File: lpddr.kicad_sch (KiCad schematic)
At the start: 2 parts, among them U1 MPFS250T-FCVG484, U11 MT53D512M32D2_WFBGA

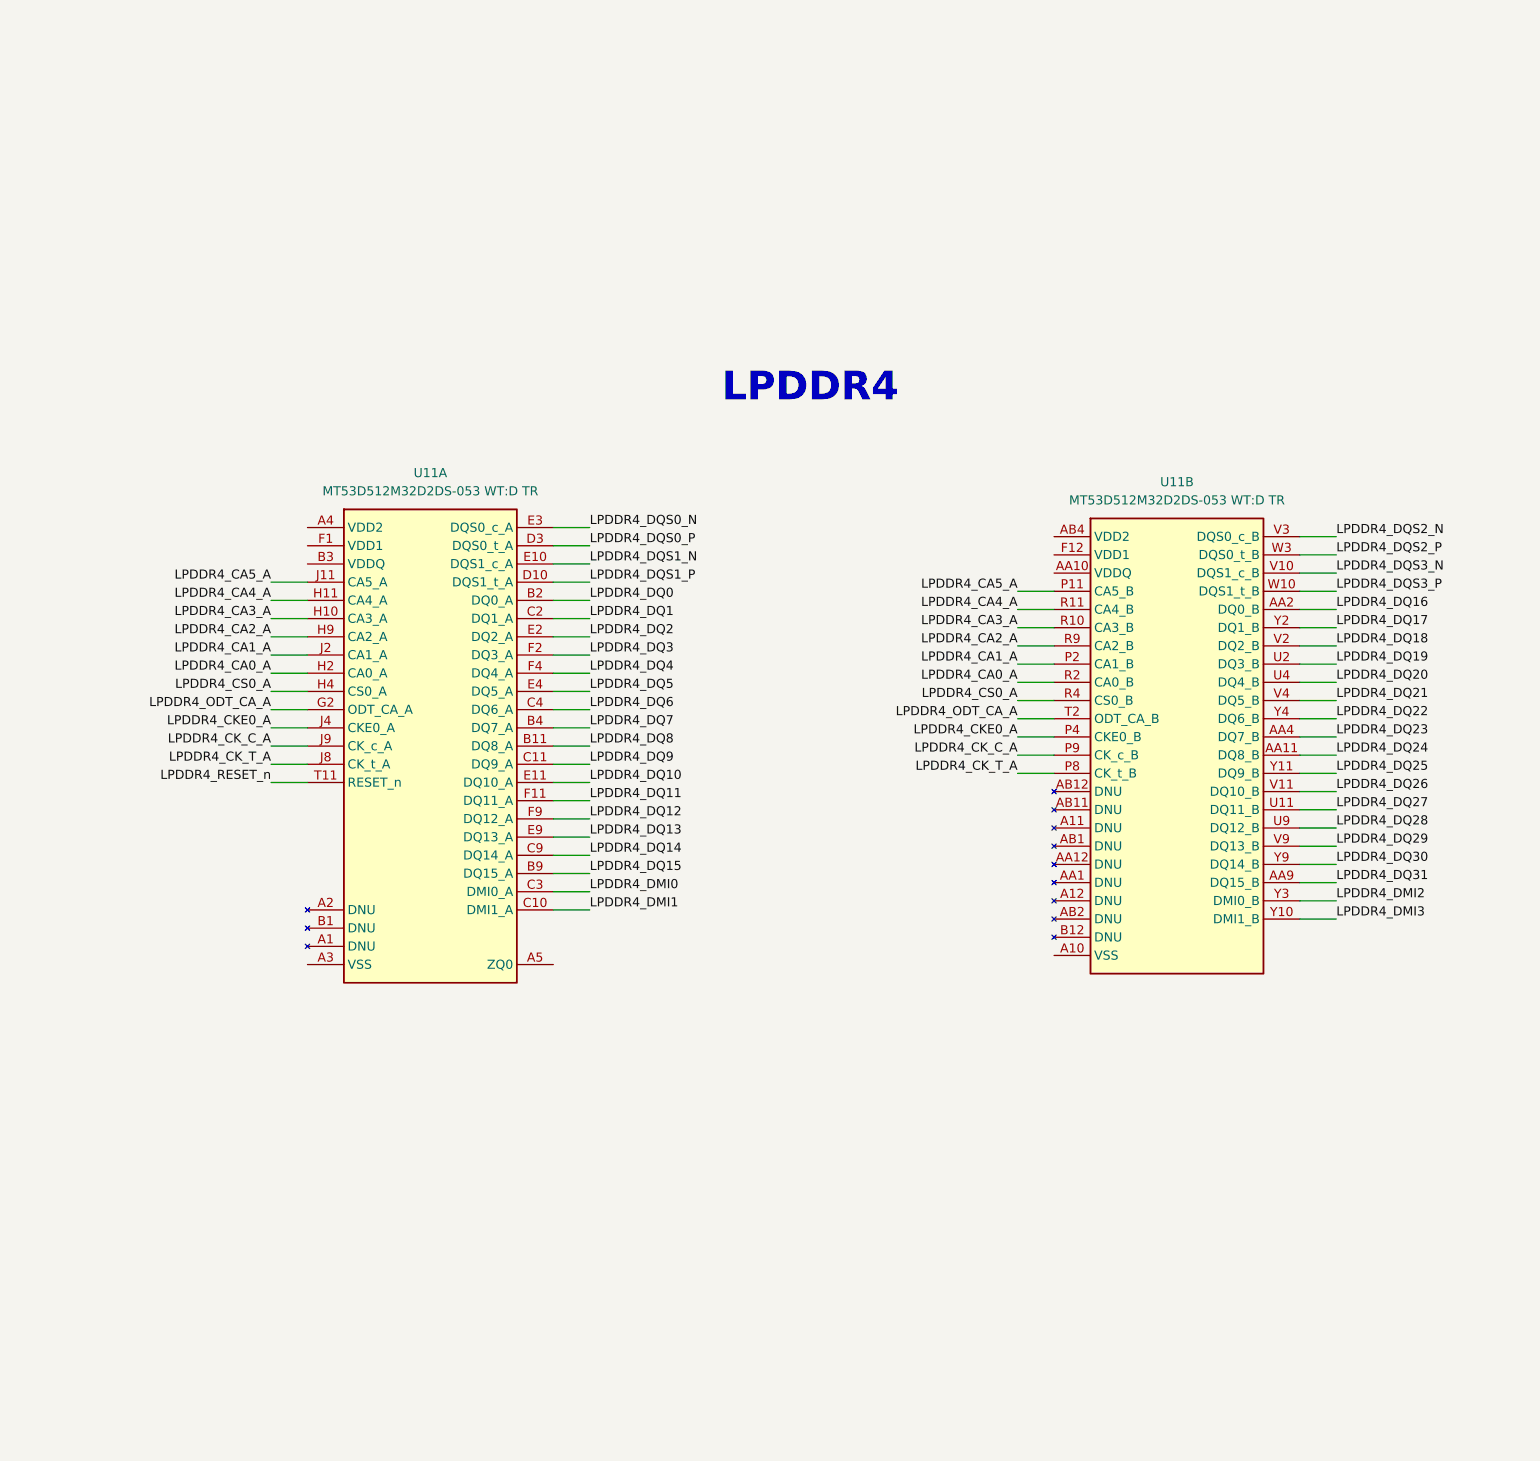
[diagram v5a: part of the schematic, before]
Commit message: [#54491] Add decoupling capacitors to LPDDR4
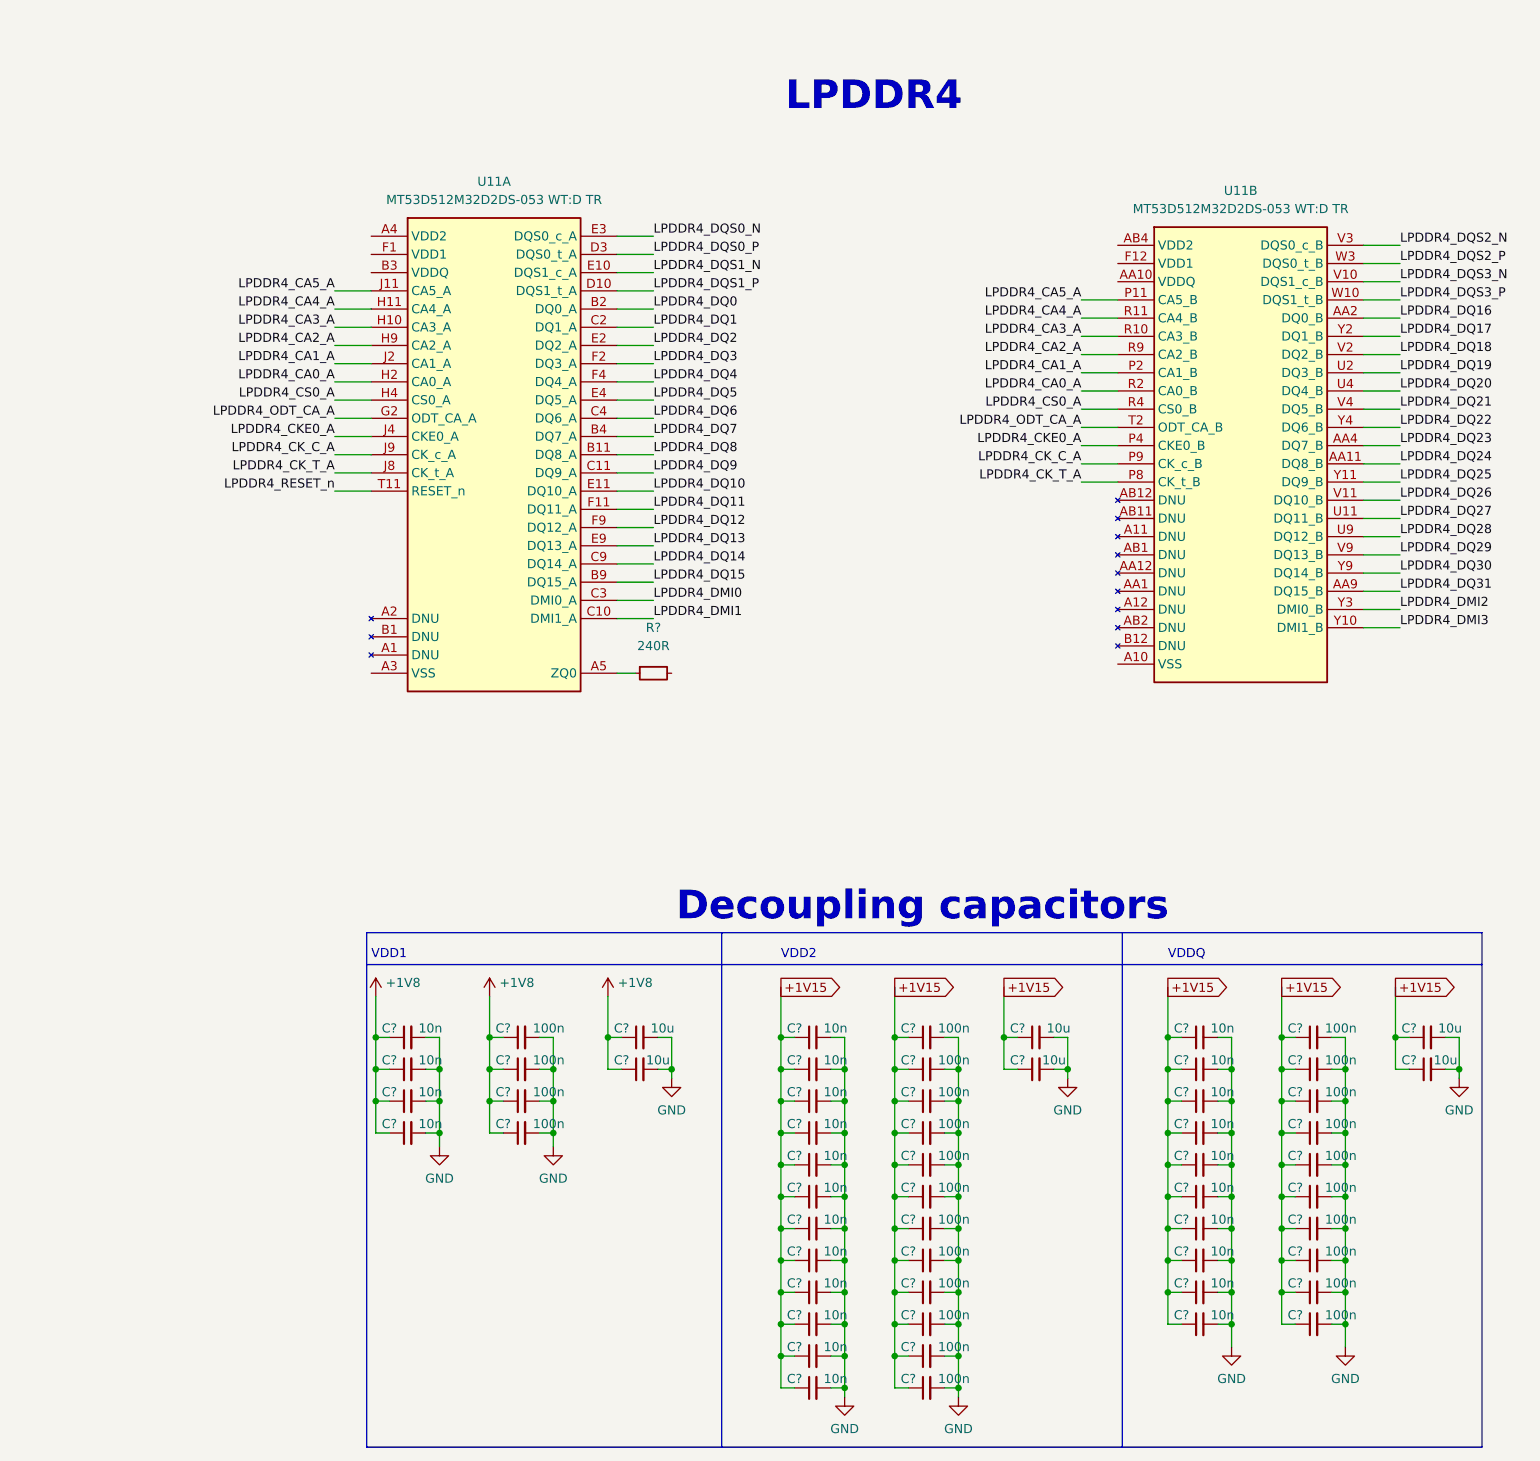
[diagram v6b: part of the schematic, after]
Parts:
- added C? (x26): C_100n_0402, antmicro-footprints:C_0402_1005Metric, symbol antmicroCapacitors0402:C_100n_0402
- added C? (x26): C_10n_0402, antmicro-footprints:C_0402_1005Metric, symbol antmicroCapacitors0402:C_10n_0402
- added C? (x6): C_10u_0402, antmicro-footprints:C_0402_1005Metric, symbol antmicroCapacitors0402:C_10u_0402
- added R?: R_240R_0402, antmicro-footprints:R_0402_1005Metric, symbol antmicroResistors0402:R_240R_0402
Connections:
- net at U11.A5 (ZQ0): now also R?.1
- new net +1V15: C?.1, C?.1, C?.1, C?.1, C?.1, C?.1, C?.1, C?.1, C?.1, C?.1, C?.1, C?.1, C?.1, C?.1, C?.1, C?.1, C?.1, C?.1, C?.1, C?.1, C?.1, C?.1, C?.1, C?.1, C?.1, C?.1, C?.1, C?.1, C?.1, C?.1, C?.1, C?.1, C?.1, C?.1, C?.1, C?.1, C?.1, C?.1, C?.1, C?.1, C?.1, C?.1, C?.1, C?.1, C?.1, C?.1, C?.1, C?.1
- new net +1V8: C?.1, C?.1, C?.1, C?.1, C?.1, C?.1, C?.1, C?.1, C?.1, C?.1
- new net GND: C?.2, C?.2, C?.2, C?.2, C?.2, C?.2, C?.2, C?.2, C?.2, C?.2, C?.2, C?.2, C?.2, C?.2, C?.2, C?.2, C?.2, C?.2, C?.2, C?.2, C?.2, C?.2, C?.2, C?.2, C?.2, C?.2, C?.2, C?.2, C?.2, C?.2, C?.2, C?.2, C?.2, C?.2, C?.2, C?.2, C?.2, C?.2, C?.2, C?.2, C?.2, C?.2, C?.2, C?.2, C?.2, C?.2, C?.2, C?.2, C?.2, C?.2, C?.2, C?.2, C?.2, C?.2, C?.2, C?.2, C?.2, C?.2
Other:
- note added: "Decoupling capacitors"
- note added: "VDD1"
- note added: "VDD2"
- note added: "VDDQ"
- moved on the sheet: U11A, U11B

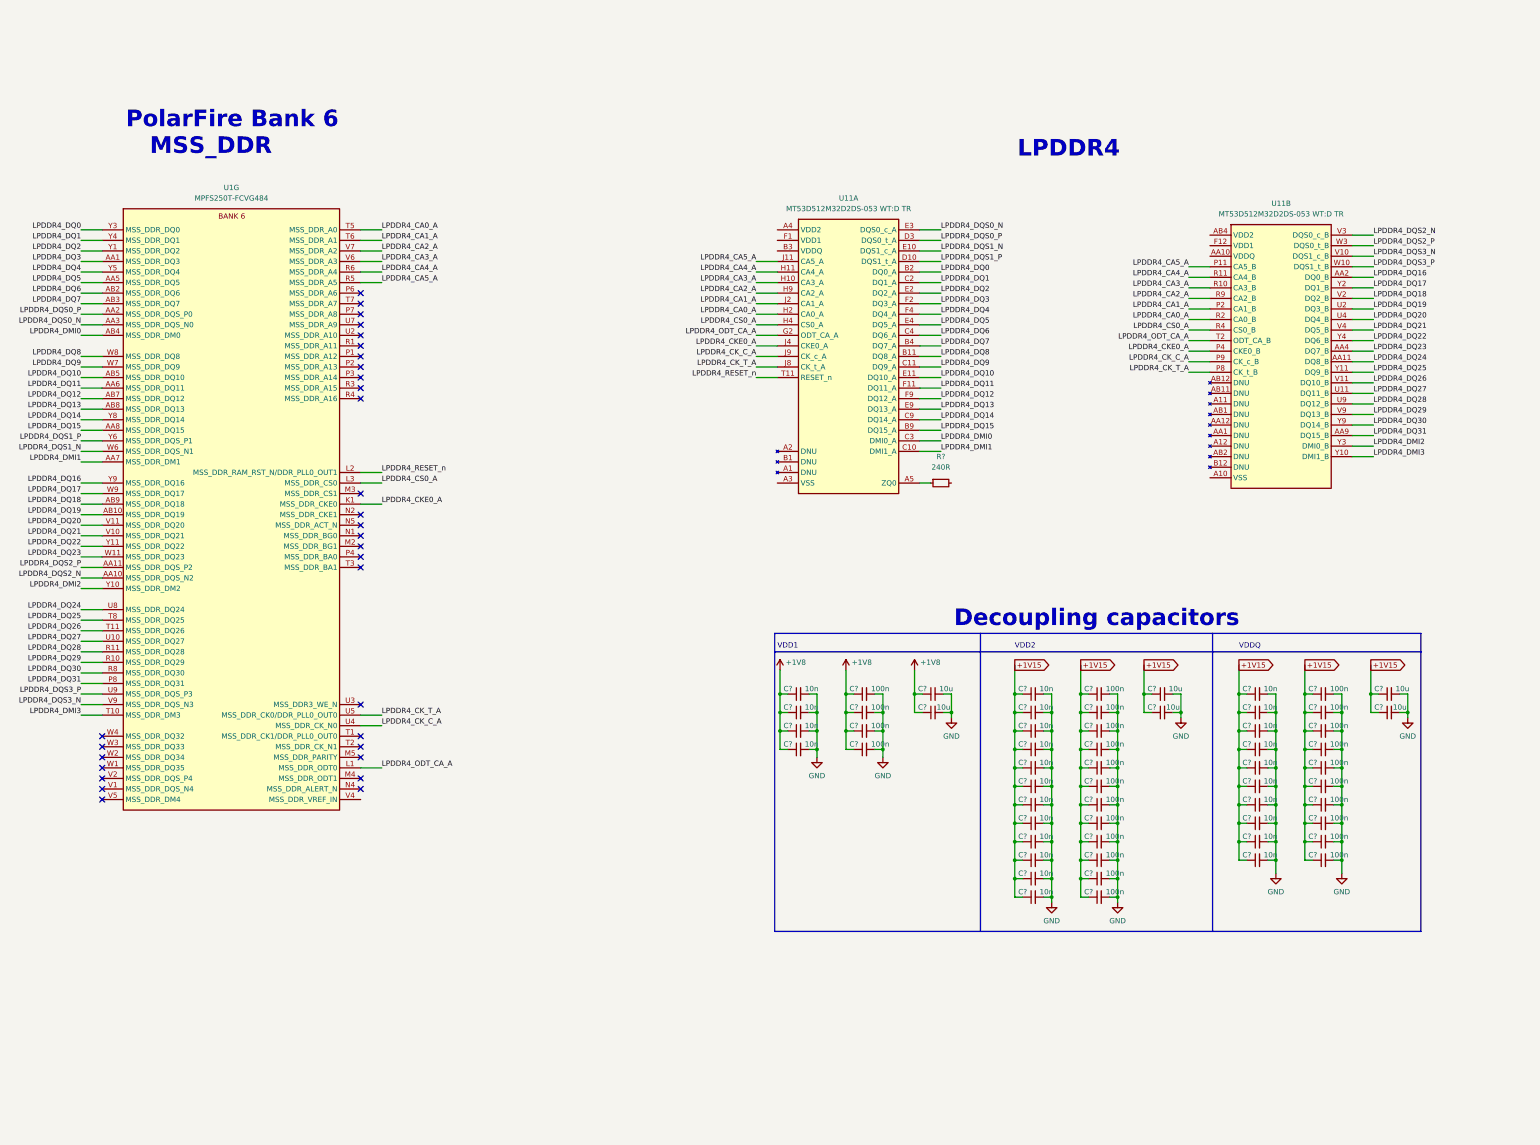
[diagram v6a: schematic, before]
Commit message: [#54491] Provide power for LPDDR4
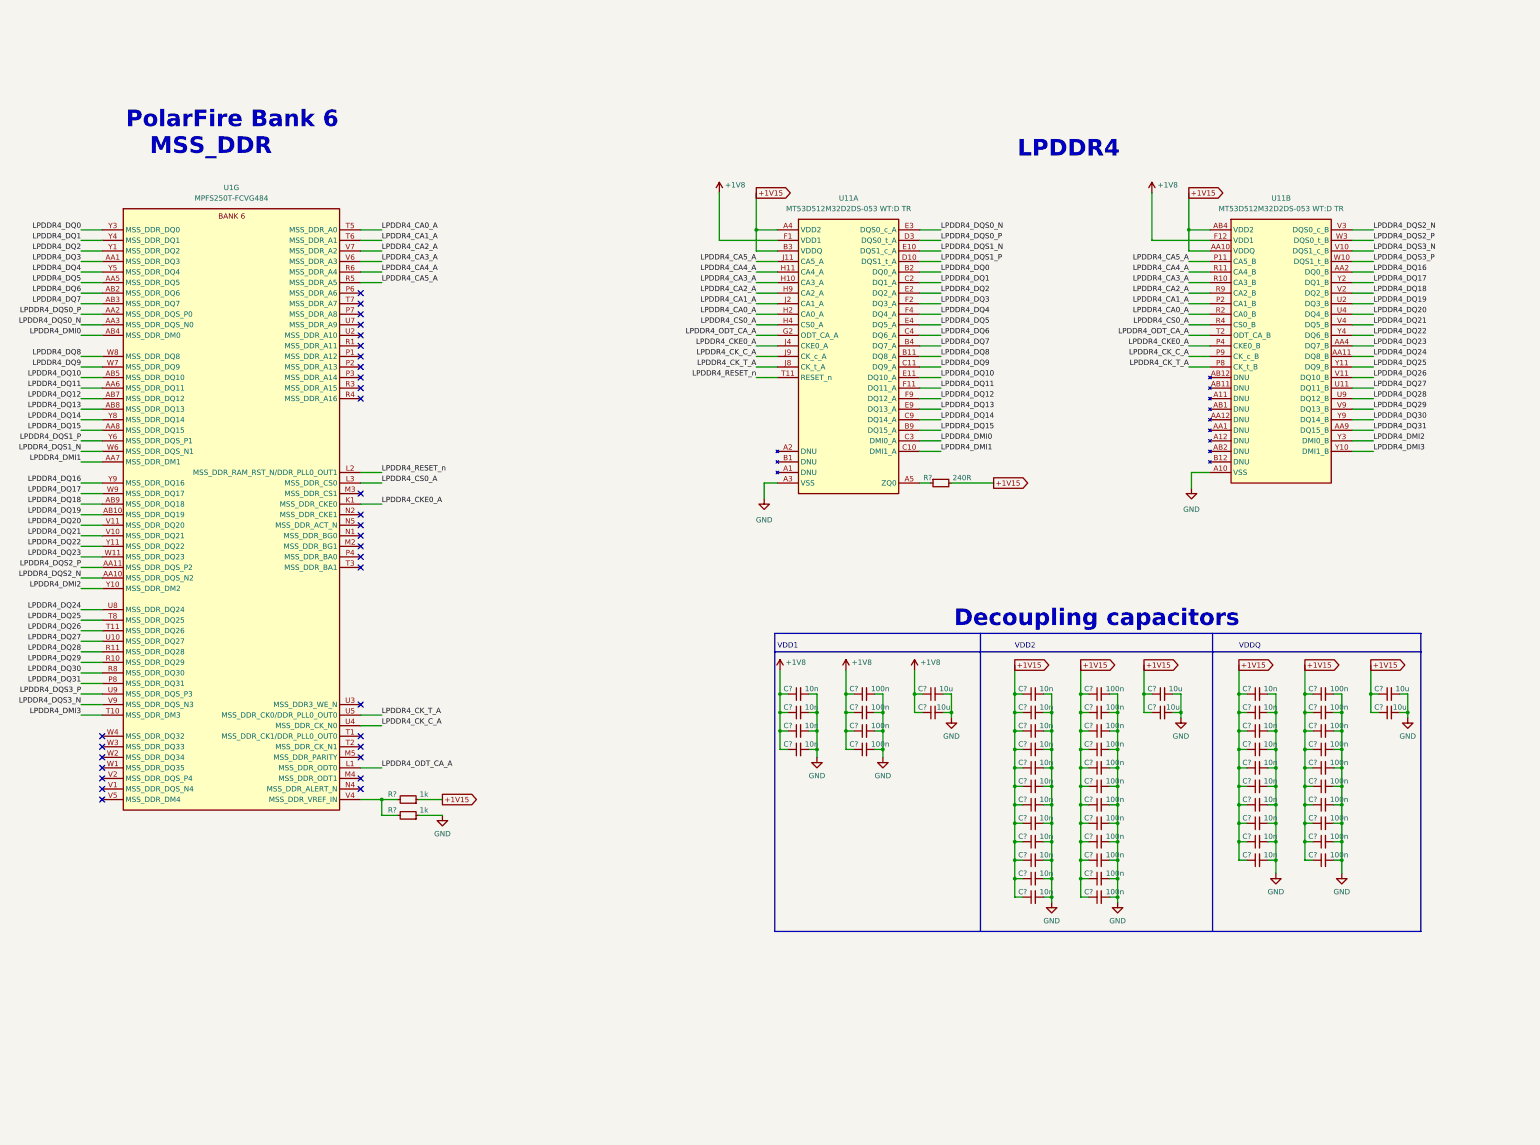
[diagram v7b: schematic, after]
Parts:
- added R? (x2): R_1k_0402, antmicro-footprints:R_0402_1005Metric, symbol antmicroResistors0402:R_1k_0402
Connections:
- net +1V15: now also R?.2, U11.A4 (VDD2), U11.A9 (VDD2), U11.AA10 (VDDQ), U11.AA3 (VDDQ), U11.AA5 (VDDQ), U11.AA8 (VDDQ), U11.AB4 (VDD2), U11.AB9 (VDD2), U11.B10 (VDDQ), U11.B3 (VDDQ), U11.B5 (VDDQ), U11.B8 (VDDQ), U11.D1 (VDDQ), U11.D12 (VDDQ), U11.D5 (VDDQ), U11.D8 (VDDQ), U11.F10 (VDDQ), U11.F3 (VDDQ), U11.F5 (VDD2), U11.F8 (VDD2), U11.H1 (VDD2), U11.H12 (VDD2), U11.H5 (VDD2), U11.H8 (VDD2), U11.K1 (VDD2), U11.K10 (VDD2), U11.K12 (VDD2), U11.K3 (VDD2), U11.N1 (VDD2), U11.N10 (VDD2), U11.N12 (VDD2), U11.N3 (VDD2), U11.R1 (VDD2), U11.R12 (VDD2), U11.R5 (VDD2), U11.R8 (VDD2), U11.U10 (VDDQ), U11.U3 (VDDQ), U11.U5 (VDD2), U11.U8 (VDD2), U11.W1 (VDDQ), U11.W12 (VDDQ), U11.W5 (VDDQ), U11.W8 (VDDQ), R?.1
- net +1V8: now also U11.F1 (VDD1), U11.F12 (VDD1), U11.G4 (VDD1), U11.G9 (VDD1), U11.T4 (VDD1), U11.T9 (VDD1), U11.U1 (VDD1), U11.U12 (VDD1)
- net GND: now also U11.A10 (VSS), U11.A3 (VSS), U11.AB10 (VSS), U11.AB3 (VSS), U11.AB5 (VSS), U11.AB8 (VSS), U11.C1 (VSS), U11.C12 (VSS), U11.C5 (VSS), U11.C8 (VSS), U11.D11 (VSS), U11.D2 (VSS), U11.D4 (VSS), U11.D9 (VSS), U11.E1 (VSS), U11.E12 (VSS), U11.E5 (VSS), U11.E8 (VSS), U11.G1 (VSS), U11.G10 (VSS), U11.G12 (VSS), U11.G3 (VSS), U11.G5 (VSS), U11.G8 (VSS), U11.J1 (VSS), U11.J10 (VSS), U11.J12 (VSS), U11.J3 (VSS), U11.K11 (VSS), U11.K2 (VSS), U11.K4 (VSS), U11.K9 (VSS), U11.N11 (VSS), U11.N2 (VSS), U11.N4 (VSS), U11.N9 (VSS), U11.P1 (VSS), U11.P10 (VSS), U11.P12 (VSS), U11.P3 (VSS), U11.T1 (VSS), U11.T10 (VSS), U11.T12 (VSS), U11.T3 (VSS), U11.T5 (VSS), U11.T8 (VSS), U11.V1 (VSS), U11.V12 (VSS), U11.V5 (VSS), U11.V8 (VSS), U11.W11 (VSS), U11.W2 (VSS), U11.W4 (VSS), U11.W9 (VSS), U11.Y1 (VSS), U11.Y12 (VSS), U11.Y5 (VSS), U11.Y8 (VSS), R?.1
- net at U1.V4 (MSS_DDR_VREF_IN): now also R?.2, R?.2
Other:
- moved on the sheet: U11B

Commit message: [#54491] Minor adjustments of labels and graphical items
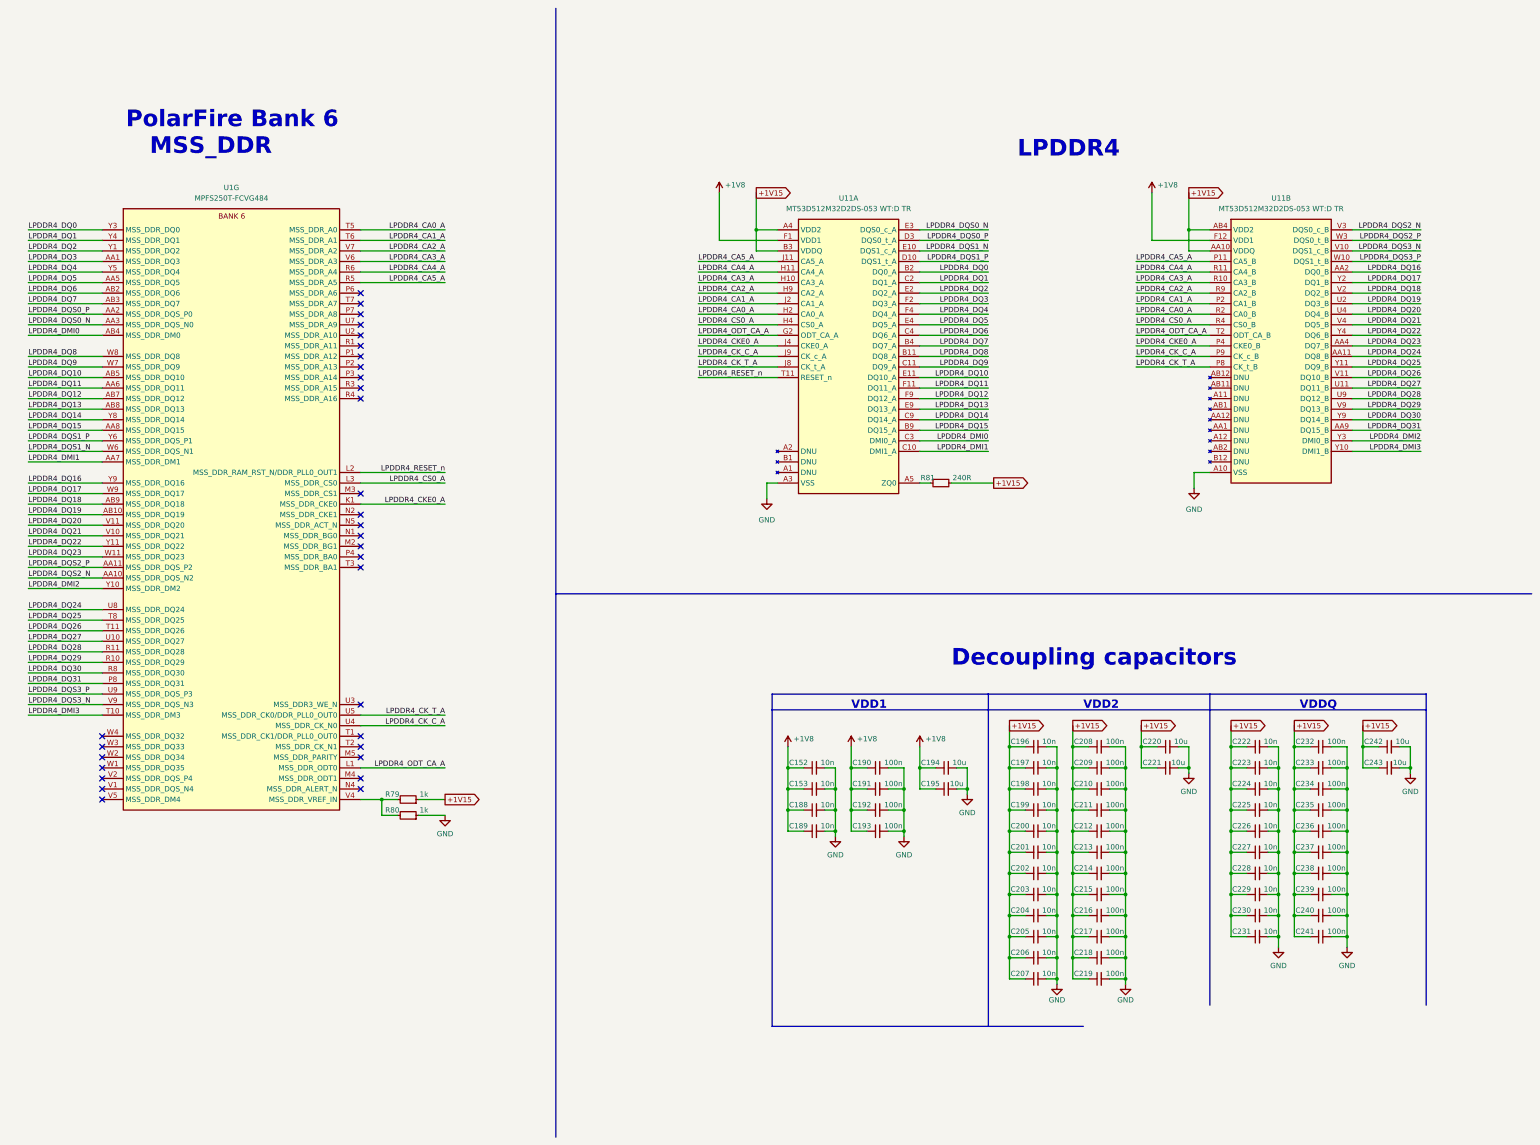
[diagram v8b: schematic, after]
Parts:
- gave numbers to parts that had none: 61
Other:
- moved on the sheet: C152, C153, C188, C189, C190, C191, C192, C193, C194, C195, C196, C197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
